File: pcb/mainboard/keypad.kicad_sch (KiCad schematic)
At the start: 4 parts, among them J800 Conn_01x28_MountingPin, SW800 EVQPUJ02K

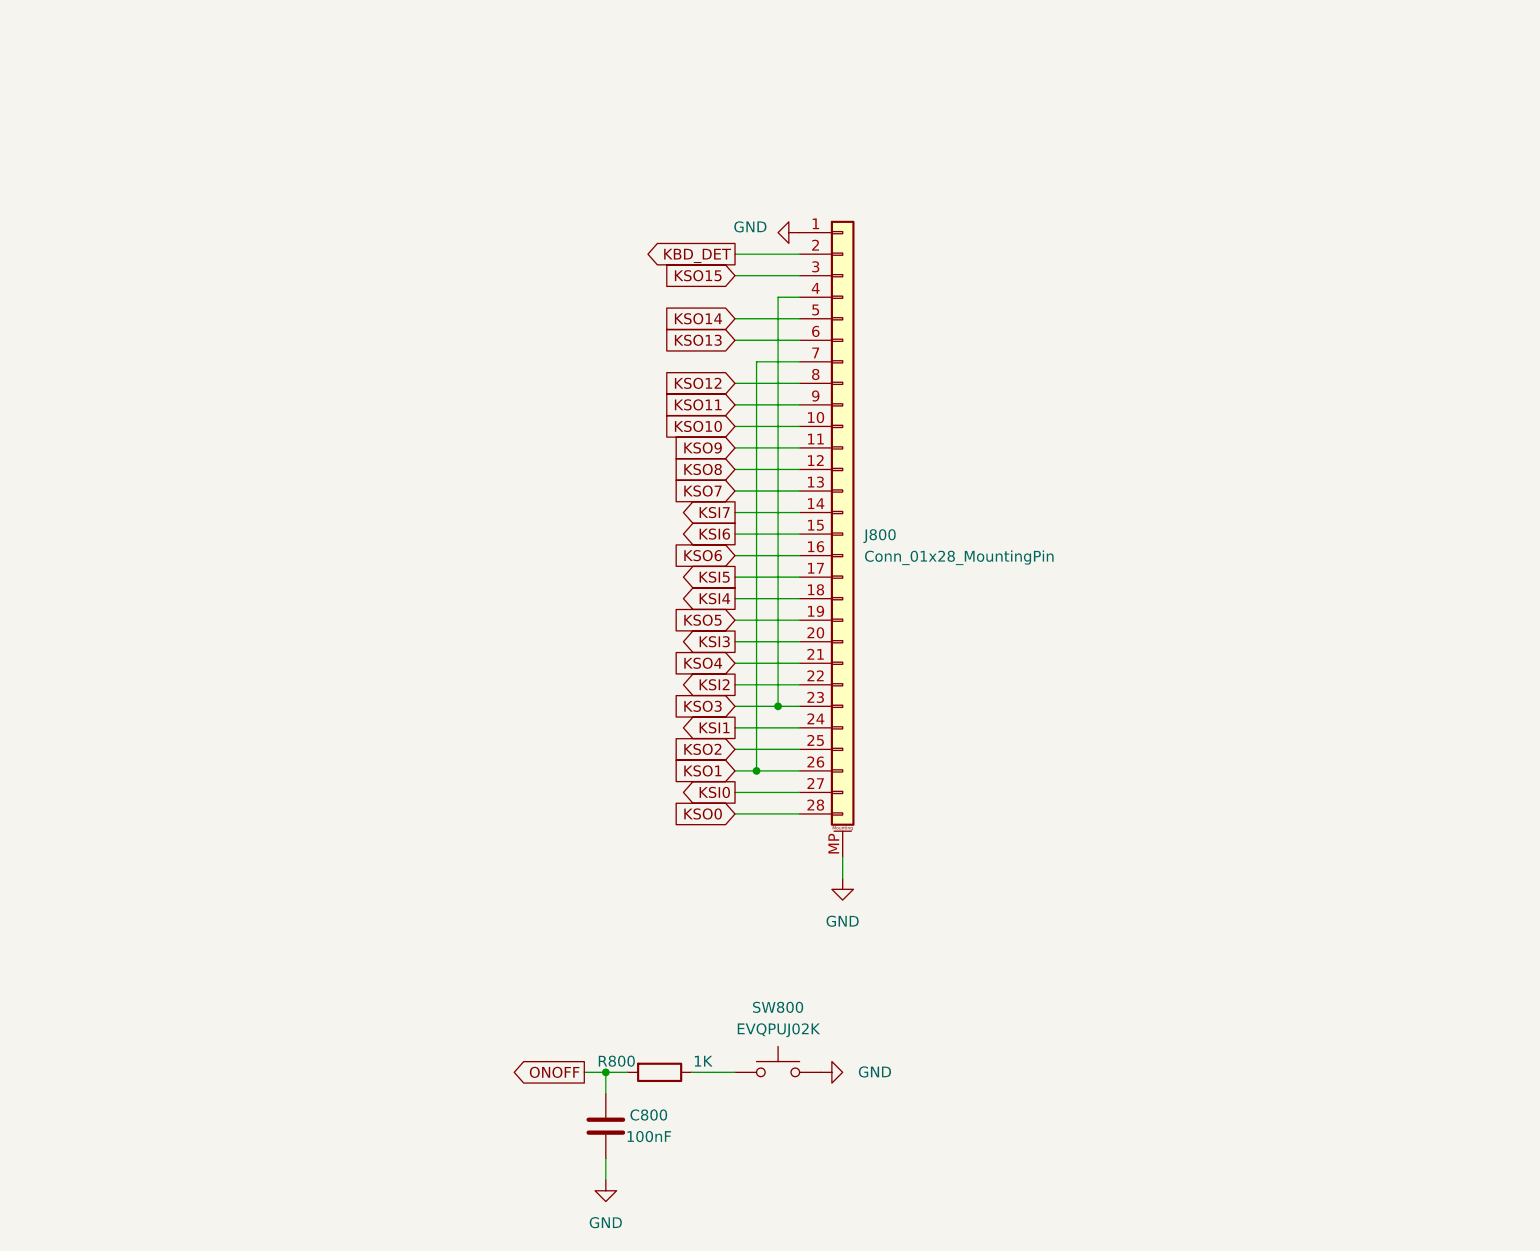
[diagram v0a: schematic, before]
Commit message: pcb: preliminary r0p1 schematics
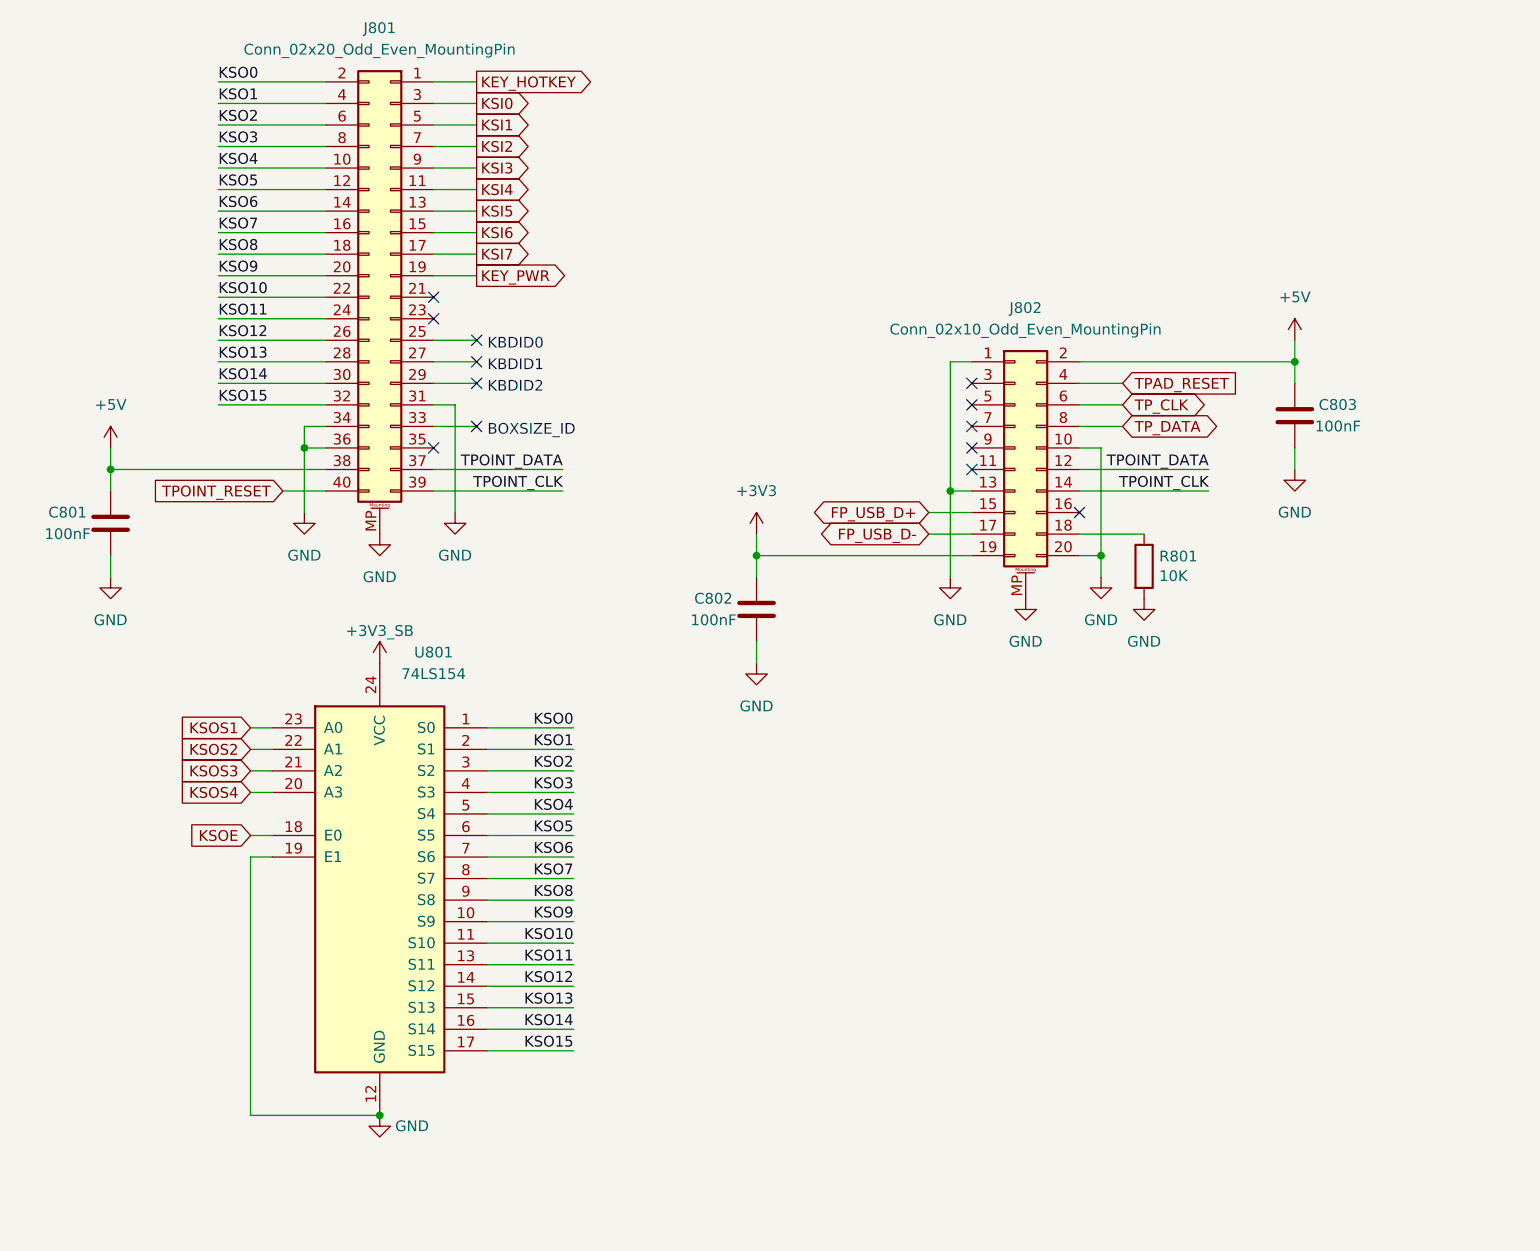
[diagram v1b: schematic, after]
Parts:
- removed C800: 100nF, Capacitor_SMD:C_0402_1005Metric, symbol Device:C
- removed J800: Conn_01x28_MountingPin, Connector_FFC-FPC:TE_2-84953-8_1x28-1MP_P1.0mm_Horizontal, symbol Connector_Generic_MountingPin:Conn_01x28_MountingPin
- removed R800: 1K, Resistor_SMD:R_0402_1005Metric, symbol Device:R
- removed SW800: EVQPUJ02K, Button_Switch_SMD:Panasonic_EVQPUJ_EVQPUA, symbol Switch:SW_Push
- added C801, C802, C803: 100nF, Capacitor_SMD:C_0402_1005Metric, symbol Device:C
- added J801: Conn_02x20_Odd_Even_MountingPin, footprints:JAE_KX14-40K5D, symbol Connector_Generic_MountingPin:Conn_02x20_Odd_Even_MountingPin
- added J802: Conn_02x10_Odd_Even_MountingPin, Connector_Hirose:Hirose_DF12_DF12E3.0-20DP-0.5V_2x10_P0.50mm_Vertical, symbol Connector_Generic_MountingPin:Conn_02x10_Odd_Even_MountingPin
- added R801: 10K, Resistor_SMD:R_0402_1005Metric, symbol Device:R
- added U801: 74LS154, Package_SO:SO-24_5.3x15mm_P1.27mm, symbol 74xx:74LS154
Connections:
- net GND: now also C801.1, C802.1, C803.1, J801.31 (Pin_31), J801.34 (Pin_34), J801.36 (Pin_36), J801.MP (MountPin), J802.1 (Pin_1), J802.10 (Pin_10), J802.13 (Pin_13), J802.20 (Pin_20), J802.MP (MountPin), R801.2, U801.12 (GND), U801.19 (E1)
- net KSI0: now also J801.3 (Pin_3)
- net KSI1: now also J801.5 (Pin_5)
- net KSI2: now also J801.7 (Pin_7)
- net KSI3: now also J801.9 (Pin_9)
- net KSI4: now also J801.11 (Pin_11)
- net KSI5: now also J801.13 (Pin_13)
- net KSI6: now also J801.15 (Pin_15)
- net KSI7: now also J801.17 (Pin_17)
- net KSO0: now also J801.2 (Pin_2), U801.1 (S0)
- net KSO1: now also J801.4 (Pin_4), U801.2 (S1)
- net KSO10: now also J801.22 (Pin_22), U801.11 (S10)
- net KSO11: now also J801.24 (Pin_24), U801.13 (S11)
- net KSO12: now also J801.26 (Pin_26), U801.14 (S12)
- net KSO13: now also J801.28 (Pin_28), U801.15 (S13)
- net KSO14: now also J801.30 (Pin_30), U801.16 (S14)
- net KSO15: now also J801.32 (Pin_32), U801.17 (S15)
- net KSO2: now also J801.6 (Pin_6), U801.3 (S2)
- net KSO3: now also J801.8 (Pin_8), U801.4 (S3)
- net KSO4: now also J801.10 (Pin_10), U801.5 (S4)
- net KSO5: now also J801.12 (Pin_12), U801.6 (S5)
- net KSO6: now also J801.14 (Pin_14), U801.7 (S6)
- net KSO7: now also J801.16 (Pin_16), U801.8 (S7)
- net KSO8: now also J801.18 (Pin_18), U801.9 (S8)
- net KSO9: now also J801.20 (Pin_20), U801.10 (S9)
- new net: J802.18 (Pin_18), R801.1
- new net +3V3: C802.2, J802.19 (Pin_19)
- new net +3V3_SB: U801.24 (VCC)
- new net +5V: C801.2, C803.2, J801.38 (Pin_38), J802.2 (Pin_2)
- new net FP_USB_D+: J802.15 (Pin_15)
- new net FP_USB_D-: J802.17 (Pin_17)
- new net KEY_HOTKEY: J801.1 (Pin_1)
- new net KEY_PWR: J801.19 (Pin_19)
- new net KSOE: U801.18 (E0)
- new net KSOS1: U801.23 (A0)
- new net KSOS2: U801.22 (A1)
- new net KSOS3: U801.21 (A2)
- new net KSOS4: U801.20 (A3)
- new net TPAD_RESET: J802.4 (Pin_4)
- new net TPOINT_CLK: J801.39 (Pin_39), J802.14 (Pin_14)
- new net TPOINT_DATA: J801.37 (Pin_37), J802.12 (Pin_12)
- new net TPOINT_RESET: J801.40 (Pin_40)
- new net TP_CLK: J802.6 (Pin_6)
- new net TP_DATA: J802.8 (Pin_8)
- no-connect marks 0 -> 13
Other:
- note added: "BOXSIZE_ID"
- note added: "KBDID0"
- note added: "KBDID1"
- note added: "KBDID2"
- company: Copyright EI-2030 2021. / Engineer: Wenting Zhang -> Copyright Modos 2021. / Engineer: Wenting Zhang
